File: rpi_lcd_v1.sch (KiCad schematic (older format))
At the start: 15 parts, among them J1 PBD-26, P1 CONN_9

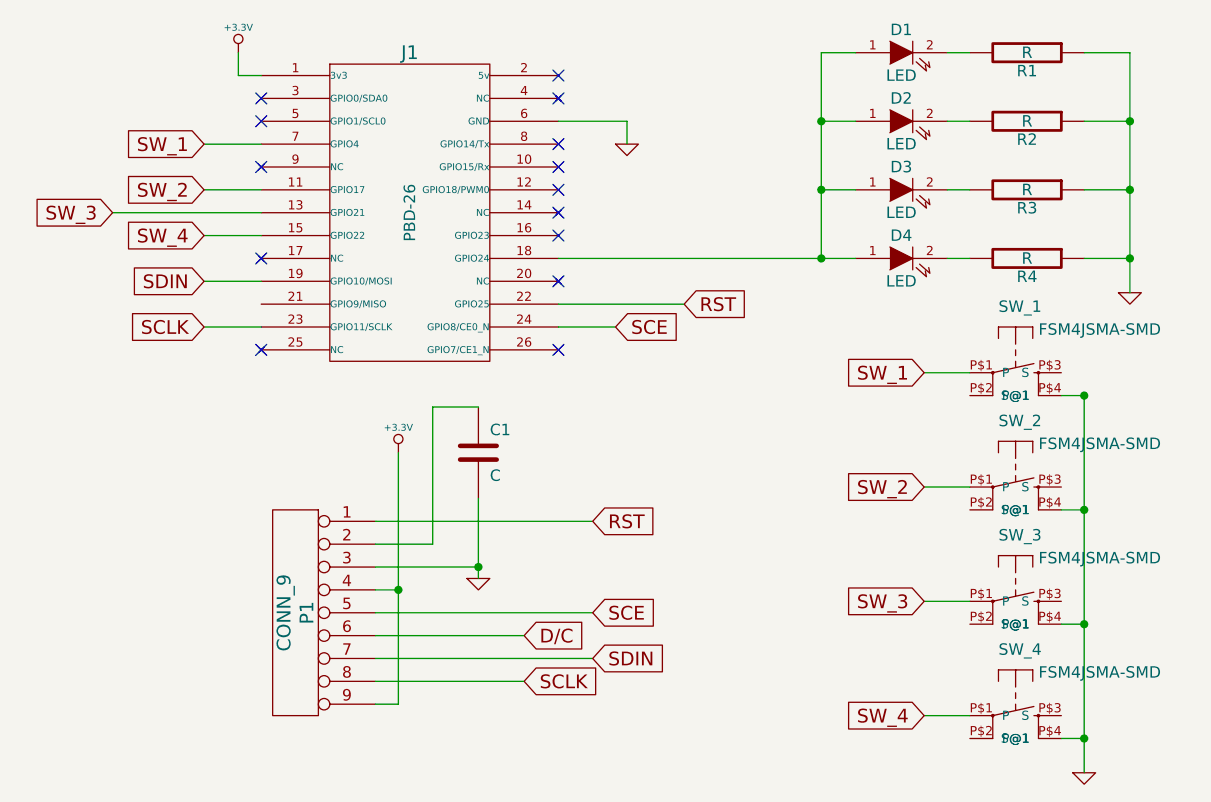
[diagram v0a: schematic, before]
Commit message: Fixed d/c line, fixed LED orientation
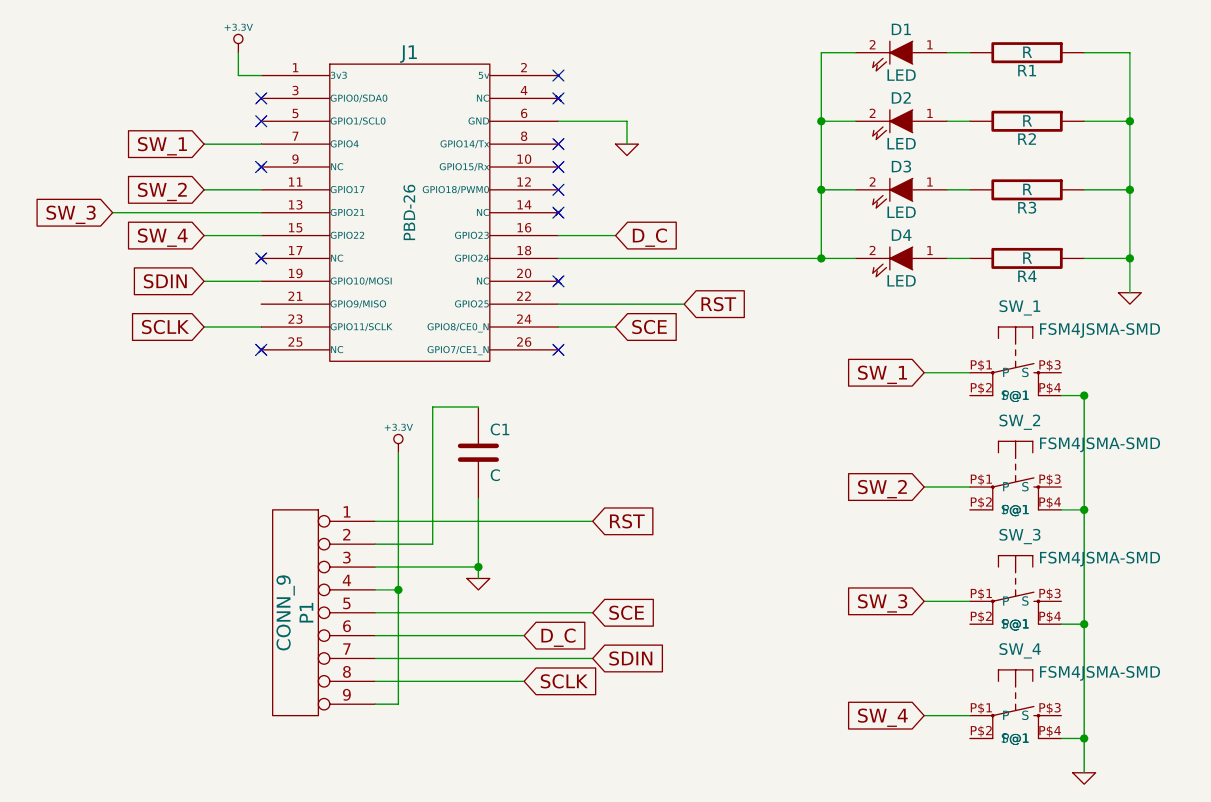
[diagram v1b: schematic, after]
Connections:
- net D/C is gone; now on net D_C: P1.6 (P6)
- net D_C: now reaches J1.16 (GPIO23)
- net at D1.2 (K): now also D2.2 (K), D3.2 (K), D4.2 (K), J1.18 (GPIO24); no longer R1.2
- net at R2.2: now also D2.1 (A); no longer D2.2 (K)
- net at R3.2: now also D3.1 (A); no longer D3.2 (K)
- net at R4.2: now also D4.1 (A); no longer D4.2 (K)
- new net: D1.1 (A), R1.2
- no-connect marks 14 -> 13
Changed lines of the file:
@@
-EESchema Schematic File Version 2  date Thu 28 Mar 2013 08:22:25 PM CDT
+EESchema Schematic File Version 2
 LIBS:power
 LIBS:device
@@
 LIBS:valves
 LIBS:rpi_lcd_v1-cache
-EELAYER 27 0
+EELAYER 24 0
 EELAYER END
 $Descr A4 11693 8268
@@
 F 3 "" H 7750 3850 60  0000 C CNN
 	1    7750 3850
-	1    0    0    -1
+	-1   0    0    -1
 $EndComp
 $Comp
@@
 F 3 "" H 7750 4150 60  0000 C CNN
 	1    7750 4150
-	1    0    0    -1
+	-1   0    0    -1
 $EndComp
 $Comp
@@
 F 3 "" H 7750 4450 60  0000 C CNN
 	1    7750 4450
-	1    0    0    -1
+	-1   0    0    -1
 $EndComp
 $Comp
@@
 F 3 "" H 7750 4750 60  0000 C CNN
 	1    7750 4750
-	1    0    0    -1
+	-1   0    0    -1
 $EndComp
 $Comp
@@
 SDIN
 Text GLabel 6100 6400 2    60   Input ~ 0
-D/C
+D_C
 Text GLabel 6400 6300 2    60   Input ~ 0
 SCE
@@
 Wire Wire Line
 	4950 4250 4700 4250
-NoConn ~ 6250 4650
 NoConn ~ 6250 4450
 NoConn ~ 6250 4350
@@
 	1    0    0    -1
 $EndComp
+Text GLabel 6500 4650 2    60   Input ~ 0
+D_C
+Wire Wire Line
+	6250 4650 6500 4650
 $EndSCHEMATC
